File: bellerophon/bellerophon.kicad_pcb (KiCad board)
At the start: 4 copper layers, 142 x 100.5 mm, 90 parts, among them Q1 ST3413A, Q2 IRLL014NPBF, Q3 IRLL014NPBF, U1 HT7350-A, U2 BNO055, U3 MPL3115A2, U4 Teensy4.0, U5 XTSD, Y1 32.768kHz

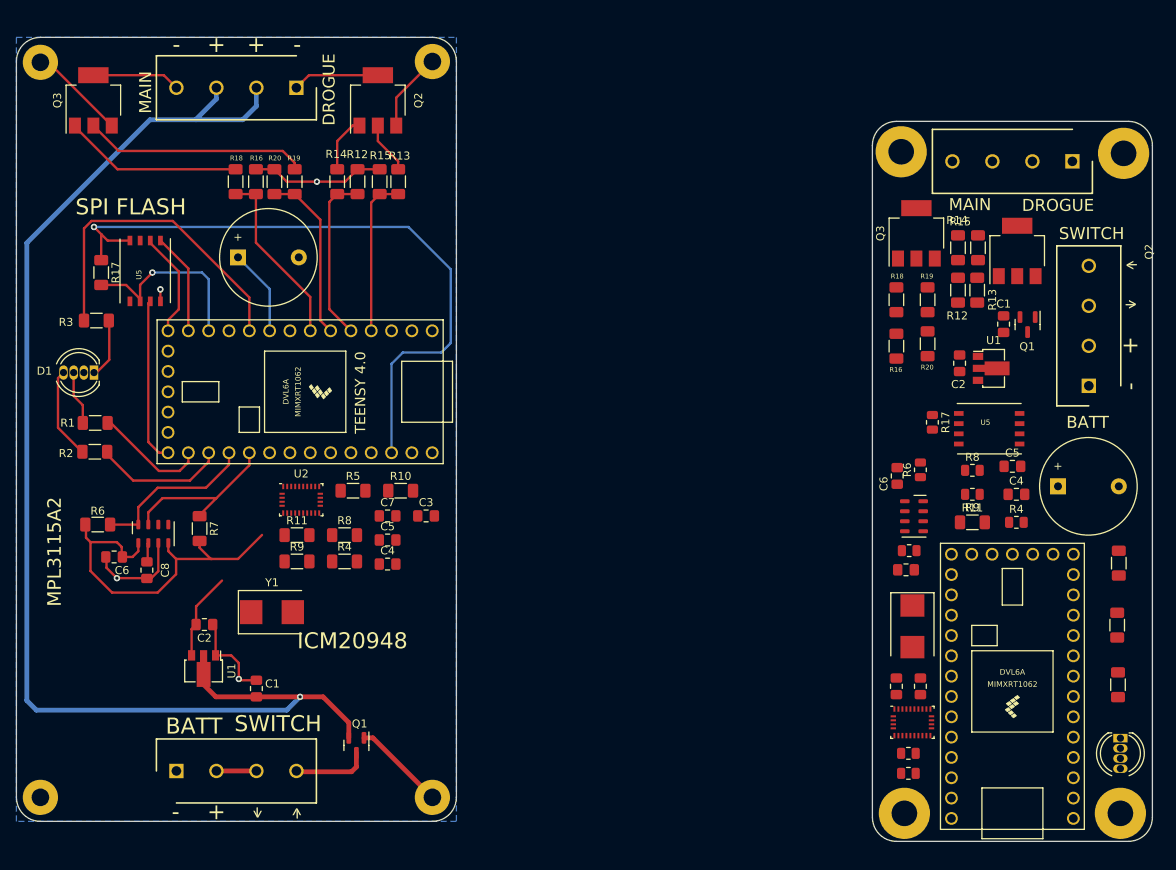
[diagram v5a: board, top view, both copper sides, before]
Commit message: remove silkscreen reference designators
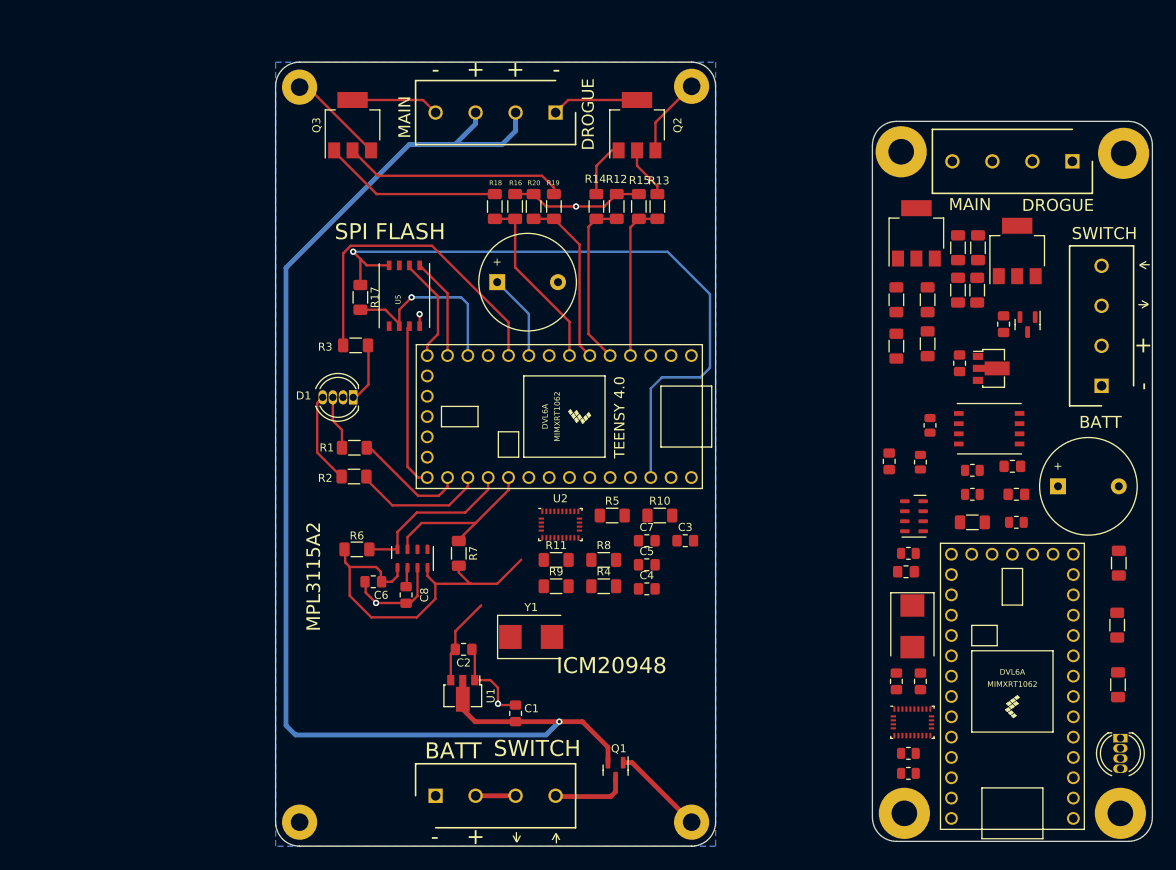
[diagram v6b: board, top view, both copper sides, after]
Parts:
- moved C1 32.5 mm to (157.9, 134.0)
- moved C2 32.5 mm to (151.4, 126.0)
- moved C3 32.5 mm to (179.1, 112.4)
- moved C4 32.5 mm to (174.3, 118.4)
- moved C5 32.5 mm to (174.3, 115.4)
- moved C6 32.5 mm to (140.1, 117.5)
- moved C7 32.5 mm to (174.3, 112.4)
- moved C8 32.5 mm to (144.2, 119.2)
- moved H1 32.5 mm to (130.9, 147.6)
- moved H2 32.5 mm to (179.9, 147.6)
- moved H3 32.5 mm to (130.9, 55.7)
- moved H4 32.5 mm to (179.9, 55.6)
- moved PYRO1 32.5 mm to (162.9, 58.9)
- moved Q1 32.5 mm to (170.4, 141.1)
- moved Q2 32.5 mm to (173.1, 60.5)
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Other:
- board size 142 x 100.5 mm -> 109.6 x 98 mm

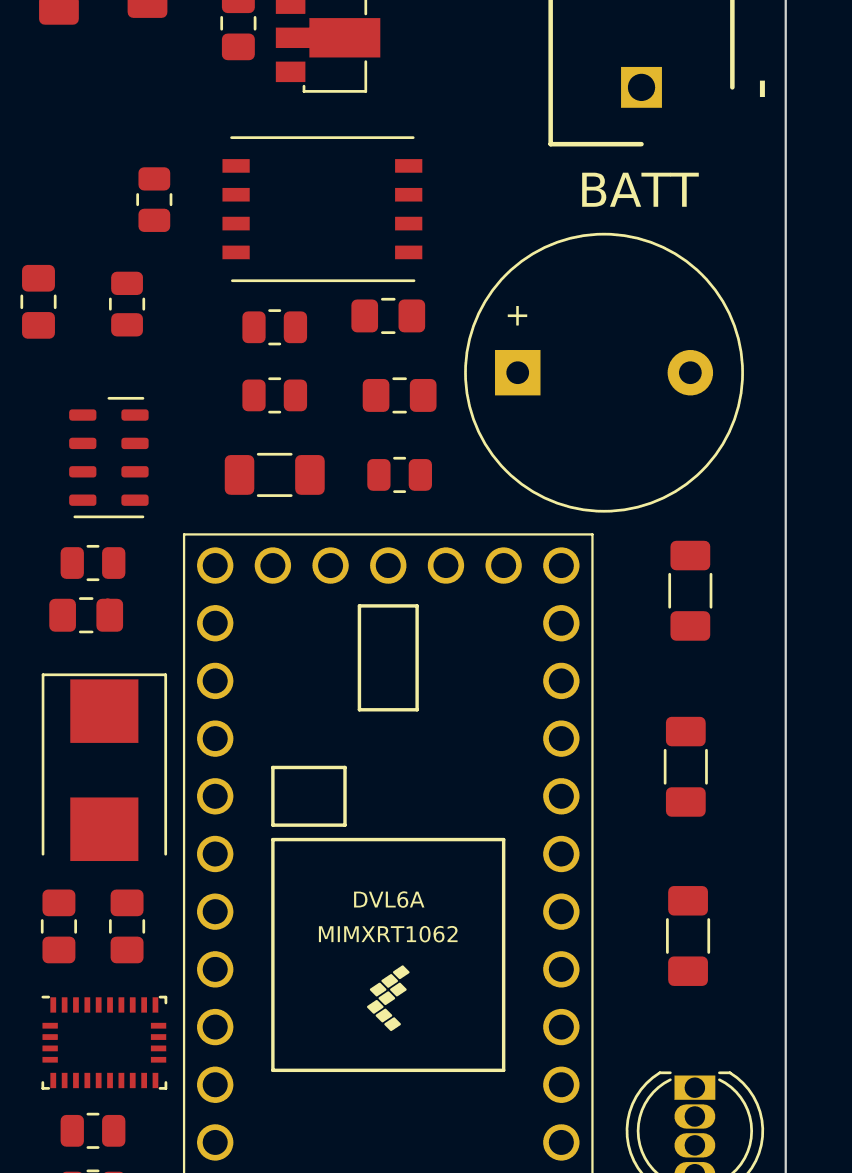
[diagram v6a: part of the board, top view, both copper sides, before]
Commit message: move nand chip to right side of teensy
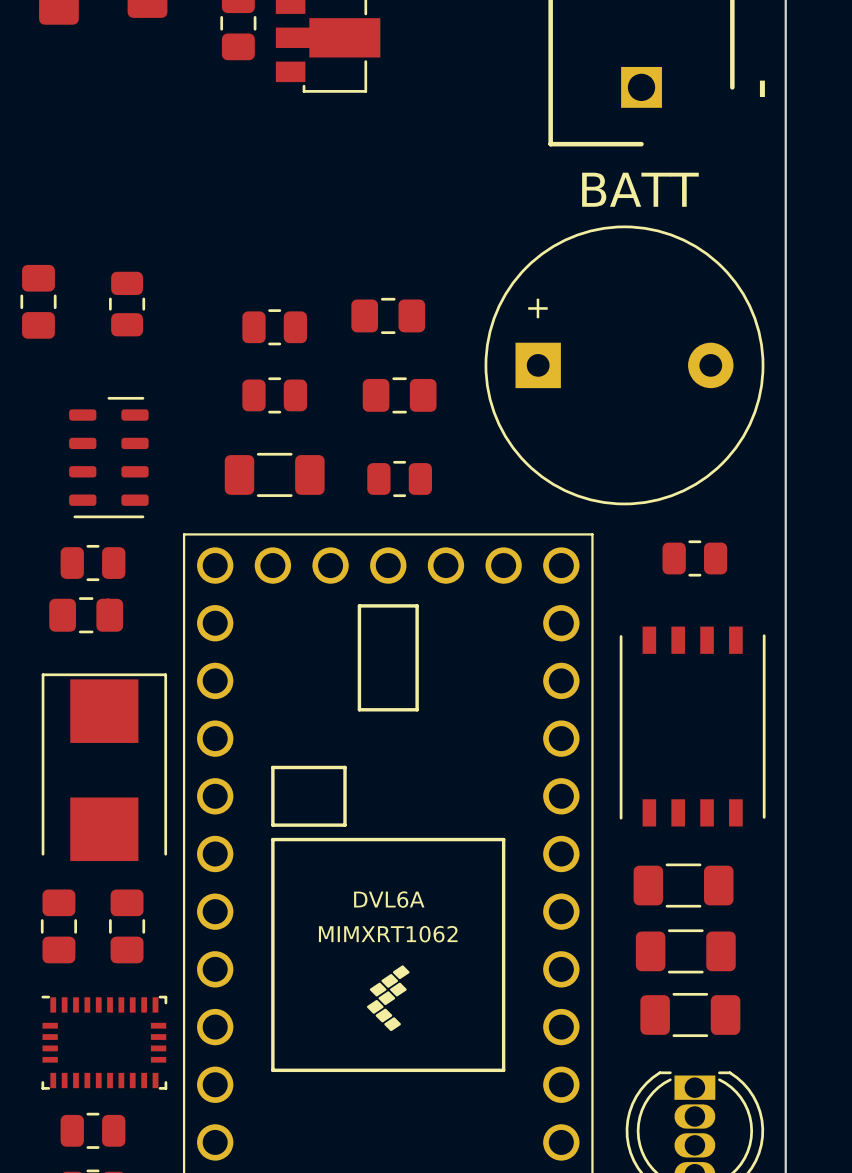
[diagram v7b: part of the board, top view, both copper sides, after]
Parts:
- moved R17 28.6 mm to (233.5, 113.8), turned to 0 degrees
- moved U5 28.0 mm to (233.4, 121.2), turned to -90 degrees
- moved R3 13.0 mm to (233.0, 128.2), turned to 180 degrees
- moved R2 8.13 mm to (233.1, 131.1), turned to 180 degrees
- moved R1 3.48 mm to (233.3, 133.9), turned to 180 degrees
- moved BZ1 0.96 mm to (226.6, 105.3)
- moved R4 0.18 mm to (220.5, 110.3)

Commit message: add step file and remove old version of board
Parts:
- removed the BZ1 at (155.6, 80.1)
- removed the C1 at (157.9, 134.0)
- removed the C2 at (151.4, 126.0)
- removed the C3 at (179.1, 112.4)
- removed the C4 at (174.3, 118.4)
- removed the C5 at (174.3, 115.4)
- removed the C6 at (140.1, 117.5)
- removed the C7 at (174.3, 112.4)
- removed the C8 at (144.2, 119.2)
- removed the D1 at (137.6, 94.5)
- removed the H1 at (130.9, 147.6)
- removed the H2 at (179.9, 147.6)
- removed the H3 at (130.9, 55.7)
- removed the H4 at (179.9, 55.6)
- removed the PYRO1 at (162.9, 58.9)
- removed the Q1 at (170.4, 141.1)
- removed the Q2 at (173.1, 60.5)
- removed the Q3 at (137.5, 60.5)
- removed the R1 at (137.8, 100.8)
- removed the R10 at (175.9, 109.3)
- removed the R11 at (163.0, 114.8)
- removed the R12 at (170.5, 70.6)
- removed the R13 at (173.3, 70.6)
- removed the R14 at (168.0, 70.6)
- removed the R15 at (175.6, 70.6)
- removed the R16 at (157.8, 70.6)
- removed the R17 at (138.5, 82.0)
- removed the R18 at (155.3, 70.6)
- removed the R19 at (162.7, 70.6)
- removed the R2 at (137.7, 104.4)
- removed the R20 at (160.2, 70.6)
- removed the R3 at (137.9, 88.0)
- removed the R4 at (168.9, 118.1)
- removed the R5 at (170.0, 109.3)
- removed the R6 at (138.1, 113.5)
- removed the R7 at (150.8, 114.0)
- removed the R8 at (168.9, 114.8)
- removed the R9 at (163.0, 118.1)
- removed the TERMINAL1 at (147.9, 144.3)
- removed the U1 at (151.3, 131.5)
- removed the U2 at (163.5, 110.4)
- removed the U3 at (145.0, 114.7)
- removed the U4 at (163.4, 96.9)
- removed the U5 at (144.0, 81.8)
- removed the Y1 at (159.8, 124.5)
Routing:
- net BATT+: track 164.3 -> 0.00 mm, vias 1 -> 0
- net +3.3V: track 131.0 -> 0.00 mm, vias 1 -> 0
- net GND: track 76.4 -> 0.60 mm, vias 4 -> 0
- net RGB3: track 40.7 -> 0.00 mm
- net Net-(PYRO1-Pad4): track 38.9 -> 0.00 mm
- net /CS: track 24.2 -> 0.00 mm, vias 1 -> 0
- net PY2: track 22.4 -> 0.00 mm
- net Net-(Q3-Pad1): track 22.4 -> 0.00 mm
- net PY2_TEST: track 21.5 -> 0.00 mm
- net /SDA1: track 21.3 -> 0.00 mm
- net PY1: track 21.2 -> 0.00 mm
- net /SCL1: track 20.8 -> 0.00 mm
- net /SCK: track 20.7 -> 0.00 mm
- net PY1_TEST: track 19.8 -> 0.00 mm
- net Net-(PYRO1-Pad1): track 17.3 -> 0.00 mm
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- removed copper zone on B.Cu, net GND
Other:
- board size 109.6 x 98 mm -> 35 x 90 mm
- board text removed: "Bellerophon"
- board text removed: "Flight Computer"
- board text removed: "ICM20948"
- board text removed: "MPL3115A2"
- board text removed: "SPI FLASH"
- board text removed: "TEENSY 4.0"
- board text removed: "UNSW ROCKETRY"
